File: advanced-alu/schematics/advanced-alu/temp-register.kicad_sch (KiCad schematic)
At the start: 11 parts

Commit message: updated documentation
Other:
- title: (none) -> Advanced Arithmetic Logic Unit - Temp Register
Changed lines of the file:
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@@
 (kicad_sch (version 20211123) (generator eeschema)
   (paper "A4")
+  (title_block
+    (title "Advanced Arithmetic Logic Unit - Temp Register")
+  )
   (junction (at 101.6 55.245) (diameter 0) (color 0 0 0 0)
   )

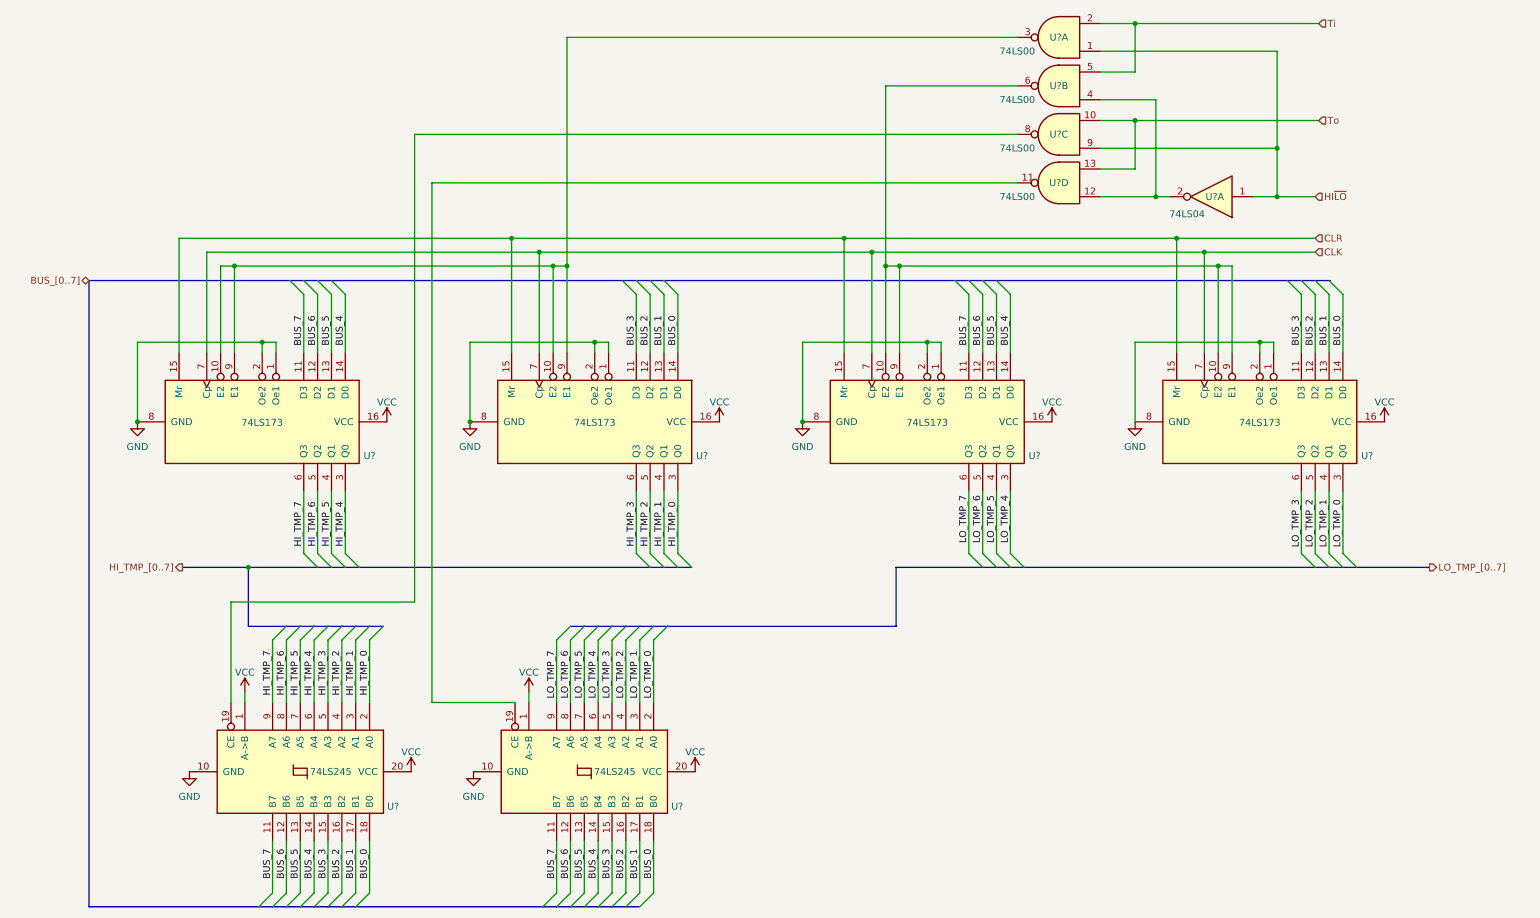
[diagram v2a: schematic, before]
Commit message: returned temp registr to being 8-bit
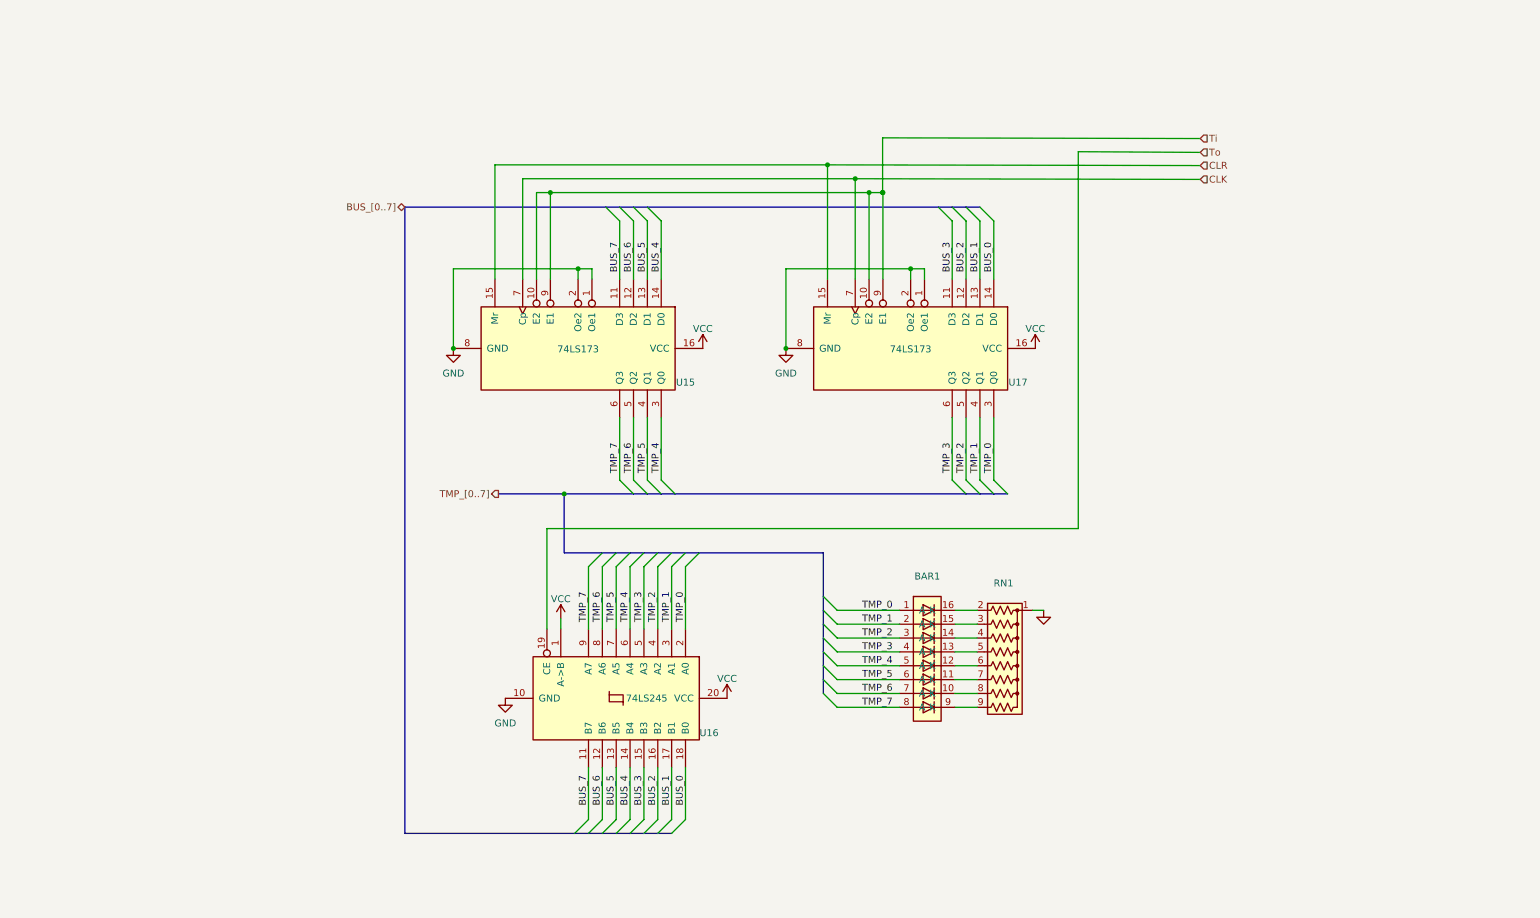
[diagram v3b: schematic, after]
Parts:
- removed U? (x4): 74LS00, symbol 74xx:74LS00
- removed U? (x2): 74LS173, symbol 74xx:74LS173
- removed U?: 74LS04, symbol 74xx:74LS04
- removed U?: 74LS245, symbol 74xx:74LS245
- added BAR1: (no value), symbol common-symbols:BarGraphLED_8P
- added RN1: (no value), symbol Device:R_Network08_US
- gave numbers to parts that had none: 3
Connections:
- net GND: now also RN1.1 (common)
- net Ti: now also U15.10 (E2), U15.9 (E1), U17.10 (E2), U17.9 (E1)
- net To: now also U16.19 (CE)
- net HI_TMP_0 renamed TMP_0
- net TMP_0: now also BAR1.1 (A)
- net HI_TMP_1 renamed TMP_1
- net TMP_1: now also BAR1.2 (A)
- net HI_TMP_2 renamed TMP_2
- net TMP_2: now also BAR1.3 (A)
- net HI_TMP_3 renamed TMP_3
- net TMP_3: now also BAR1.4 (A)
- net HI_TMP_4 renamed TMP_4
- net TMP_4: now also BAR1.5 (A)
- net HI_TMP_5 renamed TMP_5
- net TMP_5: now also BAR1.6 (A)
- net HI_TMP_6 renamed TMP_6
- net TMP_6: now also BAR1.7 (A)
- net HI_TMP_7 renamed TMP_7
- net TMP_7: now also BAR1.8 (A)
- new net: BAR1.10 (K), RN1.8 (R7)
- new net: BAR1.11 (K), RN1.7 (R6)
- new net: BAR1.12 (K), RN1.6 (R5)
- new net: BAR1.13 (K), RN1.5 (R4)
- new net: BAR1.14 (K), RN1.4 (R3)
- new net: BAR1.15 (K), RN1.3 (R2)
- new net: BAR1.16 (K), RN1.2 (R1)
- new net: BAR1.9 (K), RN1.9 (R8)
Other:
- moved on the sheet: U15, U16, U17

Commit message: tweaked design and updated documentation
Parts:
- BAR1: value (none) -> BarGraphLED_8P
- RN1: value (none) -> R_Network08_US; footprint (none) -> Resistor_THT:R_Array_SIP9
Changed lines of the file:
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@@
     (in_bom yes) (on_board yes) (fields_autoplaced)
     (property "Reference" "BAR1" (id 0) (at 177.8 117.2042 0))
-    (property "Value" "" (id 1) (at 177.8 119.7411 0))
+    (property "Value" "BarGraphLED_8P" (id 1) (at 177.8 119.7411 0))
     (property "Footprint" "" (id 2) (at 177.8 133.604 0)
       (effects (font (size 1.27 1.27)) hide)
@@
     (in_bom yes) (on_board yes) (fields_autoplaced)
     (property "Reference" "RN1" (id 0) (at 191.77 118.4742 90))
-    (property "Value" "" (id 1) (at 191.77 121.0111 90))
-    (property "Footprint" "" (id 2) (at 192.024 145.669 90)
+    (property "Value" "R_Network08_US" (id 1) (at 191.77 121.0111 90))
+    (property "Footprint" "Resistor_THT:R_Array_SIP9" (id 2) (at 192.024 145.669 90)
       (effects (font (size 1.27 1.27)) hide)
     )
@@
       (effects (font (size 1.27 1.27)) hide)
     )
-    (property "Value" "" (id 1) (at 199.136 127.8874 0))
+    (property "Value" "GND" (id 1) (at 199.136 127.8874 0))
     (property "Footprint" "" (id 2) (at 199.136 123.444 0)
       (effects (font (size 1.27 1.27)) hide)

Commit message: tweaks and layout improvements
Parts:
- renumbered BAR1 to BAR3, RN1 to RN3, U15 to U16, U16 to U17, U17 to U18
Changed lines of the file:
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@@
   (symbol (lib_id "common-symbols:BarGraphLED_8P") (at 177.8 133.604 0) (unit 1)
     (in_bom yes) (on_board yes) (fields_autoplaced)
-    (property "Reference" "BAR1" (id 0) (at 177.8 117.2042 0))
+    (property "Reference" "BAR3" (id 0) (at 177.8 117.2042 0))
     (property "Value" "BarGraphLED_8P" (id 1) (at 177.8 119.7411 0))
     (property "Footprint" "" (id 2) (at 177.8 133.604 0)
@@
   (symbol (lib_id "power:VCC") (at 136.652 75.438 0) (unit 1)
     (in_bom yes) (on_board yes) (fields_autoplaced)
-    (property "Reference" "#PWR017" (id 0) (at 136.652 79.248 0)
+    (property "Reference" "#PWR021" (id 0) (at 136.652 79.248 0)
       (effects (font (size 1.27 1.27)) hide)
     )
@@
   (symbol (lib_id "power:VCC") (at 197.612 75.438 0) (unit 1)
     (in_bom yes) (on_board yes) (fields_autoplaced)
-    (property "Reference" "#PWR020" (id 0) (at 197.612 79.248 0)
+    (property "Reference" "#PWR024" (id 0) (at 197.612 79.248 0)
       (effects (font (size 1.27 1.27)) hide)
     )
@@
   (symbol (lib_id "power:GND") (at 90.932 75.438 0) (unit 1)
     (in_bom yes) (on_board yes) (fields_autoplaced)
-    (property "Reference" "#PWR014" (id 0) (at 90.932 81.788 0)
+    (property "Reference" "#PWR018" (id 0) (at 90.932 81.788 0)
       (effects (font (size 1.27 1.27)) hide)
     )
@@
   (symbol (lib_id "Device:R_Network08_US") (at 192.024 133.604 270) (unit 1)
     (in_bom yes) (on_board yes) (fields_autoplaced)
-    (property "Reference" "RN1" (id 0) (at 191.77 118.4742 90))
+    (property "Reference" "RN3" (id 0) (at 191.77 118.4742 90))
     (property "Value" "R_Network08_US" (id 1) (at 191.77 121.0111 90))
     (property "Footprint" "Resistor_THT:R_Array_SIP9" (id 2) (at 192.024 145.669 90)
@@
   (symbol (lib_id "power:GND") (at 151.892 75.438 0) (unit 1)
     (in_bom yes) (on_board yes) (fields_autoplaced)
-    (property "Reference" "#PWR019" (id 0) (at 151.892 81.788 0)
+    (property "Reference" "#PWR023" (id 0) (at 151.892 81.788 0)
       (effects (font (size 1.27 1.27)) hide)
     )
@@
   (symbol (lib_id "power:GND") (at 100.457 139.573 0) (unit 1)
     (in_bom yes) (on_board yes) (fields_autoplaced)
-    (property "Reference" "#PWR015" (id 0) (at 100.457 145.923 0)
+    (property "Reference" "#PWR019" (id 0) (at 100.457 145.923 0)
       (effects (font (size 1.27 1.27)) hide)
     )
@@
   (symbol (lib_id "74xx:74LS173") (at 174.752 75.438 270) (unit 1)
     (in_bom yes) (on_board yes)
-    (property "Reference" "U17" (id 0) (at 194.437 81.661 90))
+    (property "Reference" "U18" (id 0) (at 194.437 81.661 90))
     (property "Value" "74LS173" (id 1) (at 174.752 75.565 90))
     (property "Footprint" "" (id 2) (at 174.752 75.438 0)
@@
   (symbol (lib_id "power:VCC") (at 110.617 124.968 0) (unit 1)
     (in_bom yes) (on_board yes) (fields_autoplaced)
-    (property "Reference" "#PWR016" (id 0) (at 110.617 128.778 0)
+    (property "Reference" "#PWR020" (id 0) (at 110.617 128.778 0)
       (effects (font (size 1.27 1.27)) hide)
     )
@@
   (symbol (lib_id "power:GND") (at 199.136 123.444 0) (unit 1)
     (in_bom yes) (on_board yes) (fields_autoplaced)
-    (property "Reference" "#PWR021" (id 0) (at 199.136 129.794 0)
+    (property "Reference" "#PWR025" (id 0) (at 199.136 129.794 0)
       (effects (font (size 1.27 1.27)) hide)
     )
@@
   (symbol (lib_id "74xx:74LS173") (at 113.792 75.438 270) (unit 1)
     (in_bom yes) (on_board yes)
-    (property "Reference" "U15" (id 0) (at 133.477 81.661 90))
+    (property "Reference" "U16" (id 0) (at 133.477 81.661 90))
     (property "Value" "74LS173" (id 1) (at 113.792 75.565 90))
     (property "Footprint" "" (id 2) (at 113.792 75.438 0)
@@
   (symbol (lib_id "74xx:74LS245") (at 120.777 139.573 270) (unit 1)
     (in_bom yes) (on_board yes)
-    (property "Reference" "U16" (id 0) (at 137.795 145.923 90))
+    (property "Reference" "U17" (id 0) (at 137.795 145.923 90))
     (property "Value" "74LS245" (id 1) (at 126.365 139.573 90))
     (property "Footprint" "" (id 2) (at 120.777 139.573 0)
@@
   (symbol (lib_id "power:VCC") (at 141.097 139.573 0) (unit 1)
     (in_bom yes) (on_board yes) (fields_autoplaced)
-    (property "Reference" "#PWR018" (id 0) (at 141.097 143.383 0)
-      (effects (font (size 1.27 1.27)) hide)
-    )
+    (property "Reference" "#PWR022" (id 0) (at 141.097 143.383 0)
+      (effects (font (size 1.27 1.27)) hide)
+    )
